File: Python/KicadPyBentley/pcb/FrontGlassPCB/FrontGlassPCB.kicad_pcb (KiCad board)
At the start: 4 copper layers, 177.3 x 82.5 mm, 69 parts

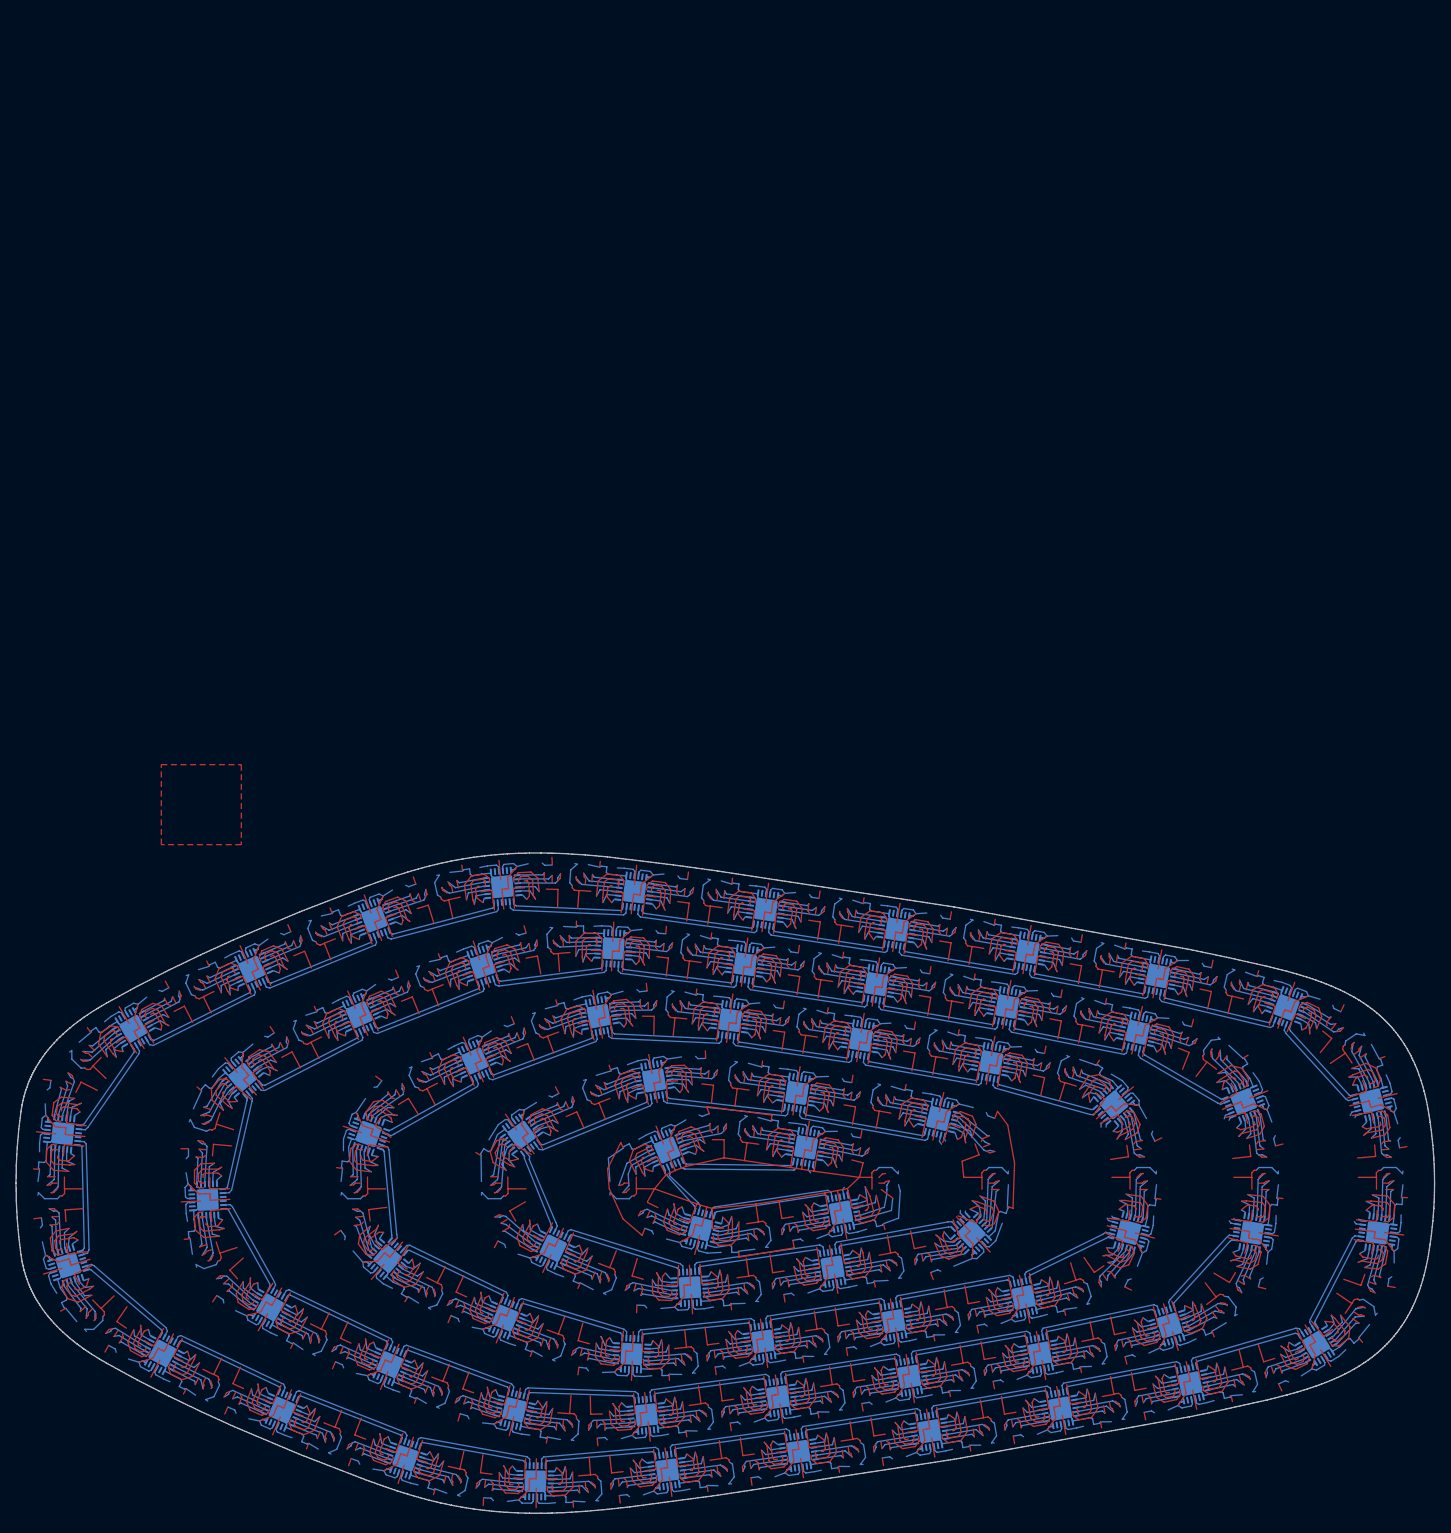
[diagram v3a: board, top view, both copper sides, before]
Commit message: added new footprints
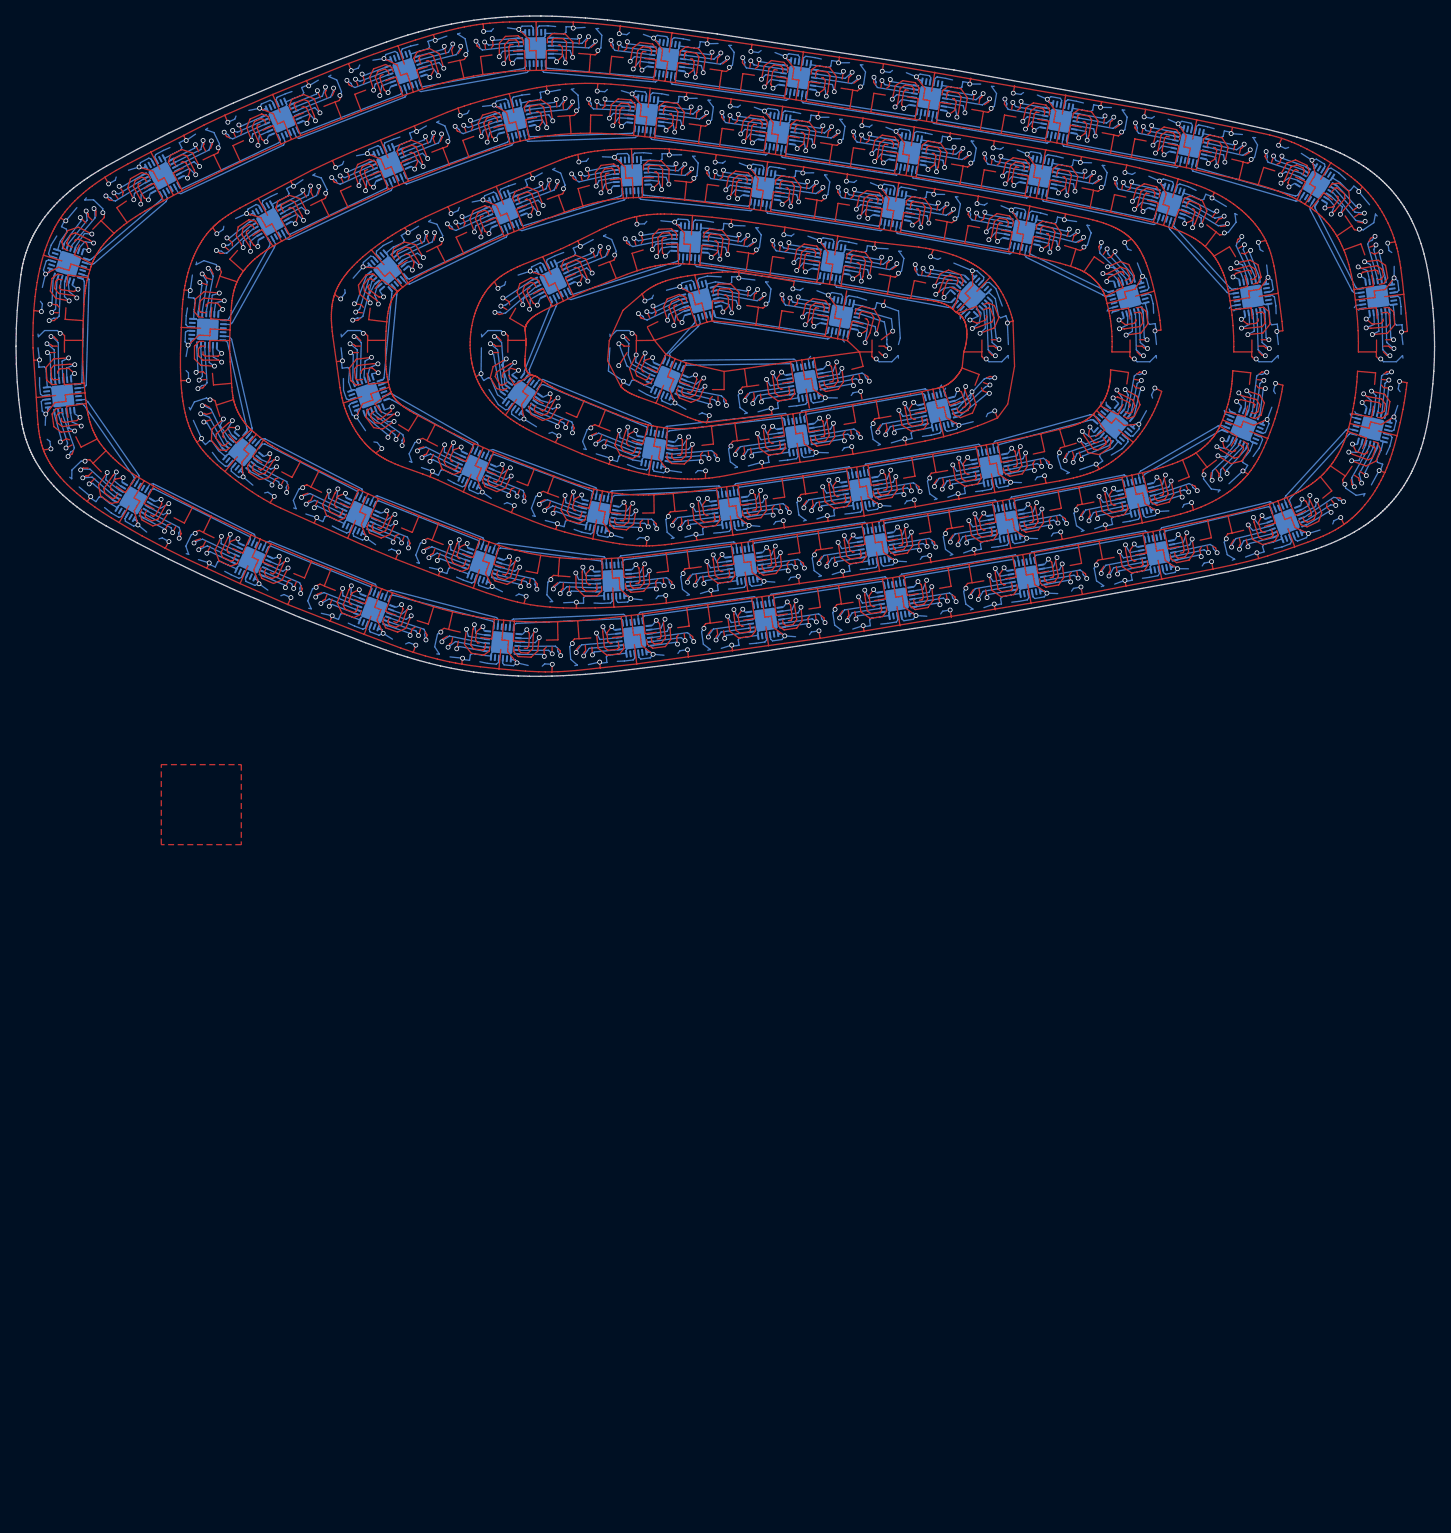
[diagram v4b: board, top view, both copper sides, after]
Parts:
- removed the REF** at (101.3, 58.6)
- removed the REF** at (107.8, 66.6)
- removed the REF** at (91.5, 69.6)
- removed the REF** at (75.2, 72.1)
- removed the REF** at (58.8, 73.7)
- removed the REF** at (43.0, 69.2)
- removed the REF** at (28.3, 61.8)
- removed the REF** at (25.9, 46.2)
- removed the REF** at (39.2, 37.0)
- removed the REF** at (54.7, 31.4)
- removed the REF** at (71.1, 31.9)
- removed the REF** at (83.9, 62.9)
- removed the REF** at (87.5, 34.4)
- removed the REF** at (103.7, 37.2)
- removed the REF** at (119.1, 42.5)
- removed the REF** at (136.3, 58.5)
- removed the REF** at (126.0, 70.1)
- removed the REF** at (109.8, 73.6)
- removed the REF** at (93.5, 76.5)
- removed the REF** at (77.1, 79.1)
- removed the REF** at (60.6, 81.3)
- removed the REF** at (44.1, 80.6)
- removed the REF** at (66.1, 65.4)
- removed the REF** at (28.6, 75.0)
- removed the REF** at (13.6, 67.8)
- removed the REF** at (5.79, 54.4)
- removed the REF** at (10.2, 39.1)
- removed the REF** at (24.8, 31.3)
- removed the REF** at (40.2, 25.1)
- removed the REF** at (56.5, 23.0)
- removed the REF** at (73.0, 25.0)
- removed the REF** at (89.4, 27.4)
- removed the REF** at (105.7, 30.2)
- removed the REF** at (49.0, 60.5)
- removed the REF** at (122.0, 33.5)
- removed the REF** at (135.3, 42.1)
- removed the REF** at (152.0, 58.5)
- removed the REF** at (144.4, 72.5)
- removed the REF** at (128.6, 77.4)
- removed the REF** at (112.3, 80.5)
- removed the REF** at (96.0, 83.3)
- removed the REF** at (79.7, 85.9)
- removed the REF** at (63.3, 88.2)
- removed the REF** at (46.8, 89.6)
- removed the REF** at (45.0, 46.3)
- removed the REF** at (30.5, 86.7)
- removed the REF** at (15.1, 80.7)
- removed the REF** at (0.14, 73.6)
- removed the REF** at (-11.6, 62.6)
- removed the REF** at (-12.3, 46.1)
- removed the REF** at (-3.49, 33.0)
- removed the REF** at (11.3, 25.6)
- removed the REF** at (26.6, 19.3)
- removed the REF** at (42.6, 15.3)
- removed the REF** at (59.2, 15.9)
- removed the REF** at (61.6, 39.5)
- removed the REF** at (75.6, 18.1)
- removed the REF** at (91.9, 20.6)
- removed the REF** at (108.3, 23.4)
- removed the REF** at (124.6, 26.4)
- removed the REF** at (140.6, 30.4)
- removed the REF** at (151.3, 42.0)
- removed the REF** at (85.0, 56.0)
- removed the REF** at (67.4, 58.0)
- removed the REF** at (63.2, 48.2)
- removed the REF** at (80.6, 47.8)
- removed the REF** at (79.5, 41.0)
- removed the REF** at (97.2, 44.2)
- removed the REF** at (120.9, 58.4)
- added REF**: Texas_RGE0024H_EP2.7x2.7mm, Texas_RGE0024H_EP2.7x2.7mm, B.Cu at (101.3, -58.6)
- added REF**: Texas_RGE0024H_EP2.7x2.7mm, Texas_RGE0024H_EP2.7x2.7mm, B.Cu at (107.8, -66.6)
- added REF**: Texas_RGE0024H_EP2.7x2.7mm, Texas_RGE0024H_EP2.7x2.7mm, B.Cu at (91.5, -69.6)
- added REF**: Texas_RGE0024H_EP2.7x2.7mm, Texas_RGE0024H_EP2.7x2.7mm, B.Cu at (75.2, -72.1)
- added REF**: Texas_RGE0024H_EP2.7x2.7mm, Texas_RGE0024H_EP2.7x2.7mm, B.Cu at (58.8, -73.7)
- added REF**: Texas_RGE0024H_EP2.7x2.7mm, Texas_RGE0024H_EP2.7x2.7mm, B.Cu at (43.0, -69.2)
- added REF**: Texas_RGE0024H_EP2.7x2.7mm, Texas_RGE0024H_EP2.7x2.7mm, B.Cu at (28.3, -61.8)
- added REF**: Texas_RGE0024H_EP2.7x2.7mm, Texas_RGE0024H_EP2.7x2.7mm, B.Cu at (25.9, -46.2)
- added REF**: Texas_RGE0024H_EP2.7x2.7mm, Texas_RGE0024H_EP2.7x2.7mm, B.Cu at (39.2, -37.0)
- added REF**: Texas_RGE0024H_EP2.7x2.7mm, Texas_RGE0024H_EP2.7x2.7mm, B.Cu at (54.7, -31.4)
- added REF**: Texas_RGE0024H_EP2.7x2.7mm, Texas_RGE0024H_EP2.7x2.7mm, B.Cu at (71.1, -31.9)
- added REF**: Texas_RGE0024H_EP2.7x2.7mm, Texas_RGE0024H_EP2.7x2.7mm, B.Cu at (83.9, -62.9)
- added REF**: Texas_RGE0024H_EP2.7x2.7mm, Texas_RGE0024H_EP2.7x2.7mm, B.Cu at (87.5, -34.4)
- added REF**: Texas_RGE0024H_EP2.7x2.7mm, Texas_RGE0024H_EP2.7x2.7mm, B.Cu at (103.7, -37.2)
- added REF**: Texas_RGE0024H_EP2.7x2.7mm, Texas_RGE0024H_EP2.7x2.7mm, B.Cu at (119.1, -42.5)
- added REF**: Texas_RGE0024H_EP2.7x2.7mm, Texas_RGE0024H_EP2.7x2.7mm, B.Cu at (136.3, -58.5)
- added REF**: Texas_RGE0024H_EP2.7x2.7mm, Texas_RGE0024H_EP2.7x2.7mm, B.Cu at (126.0, -70.1)
- added REF**: Texas_RGE0024H_EP2.7x2.7mm, Texas_RGE0024H_EP2.7x2.7mm, B.Cu at (109.8, -73.6)
- added REF**: Texas_RGE0024H_EP2.7x2.7mm, Texas_RGE0024H_EP2.7x2.7mm, B.Cu at (93.5, -76.5)
- added REF**: Texas_RGE0024H_EP2.7x2.7mm, Texas_RGE0024H_EP2.7x2.7mm, B.Cu at (77.1, -79.1)
- added REF**: Texas_RGE0024H_EP2.7x2.7mm, Texas_RGE0024H_EP2.7x2.7mm, B.Cu at (60.6, -81.3)
- added REF**: Texas_RGE0024H_EP2.7x2.7mm, Texas_RGE0024H_EP2.7x2.7mm, B.Cu at (44.1, -80.6)
- added REF**: Texas_RGE0024H_EP2.7x2.7mm, Texas_RGE0024H_EP2.7x2.7mm, B.Cu at (66.1, -65.4)
- added REF**: Texas_RGE0024H_EP2.7x2.7mm, Texas_RGE0024H_EP2.7x2.7mm, B.Cu at (28.6, -75.0)
- added REF**: Texas_RGE0024H_EP2.7x2.7mm, Texas_RGE0024H_EP2.7x2.7mm, B.Cu at (13.6, -67.8)
- added REF**: Texas_RGE0024H_EP2.7x2.7mm, Texas_RGE0024H_EP2.7x2.7mm, B.Cu at (5.79, -54.4)
- added REF**: Texas_RGE0024H_EP2.7x2.7mm, Texas_RGE0024H_EP2.7x2.7mm, B.Cu at (10.2, -39.1)
- added REF**: Texas_RGE0024H_EP2.7x2.7mm, Texas_RGE0024H_EP2.7x2.7mm, B.Cu at (24.8, -31.3)
- added REF**: Texas_RGE0024H_EP2.7x2.7mm, Texas_RGE0024H_EP2.7x2.7mm, B.Cu at (40.2, -25.1)
- added REF**: Texas_RGE0024H_EP2.7x2.7mm, Texas_RGE0024H_EP2.7x2.7mm, B.Cu at (56.5, -23.0)
- added REF**: Texas_RGE0024H_EP2.7x2.7mm, Texas_RGE0024H_EP2.7x2.7mm, B.Cu at (73.0, -25.0)
- added REF**: Texas_RGE0024H_EP2.7x2.7mm, Texas_RGE0024H_EP2.7x2.7mm, B.Cu at (89.4, -27.4)
- added REF**: Texas_RGE0024H_EP2.7x2.7mm, Texas_RGE0024H_EP2.7x2.7mm, B.Cu at (105.7, -30.2)
- added REF**: Texas_RGE0024H_EP2.7x2.7mm, Texas_RGE0024H_EP2.7x2.7mm, B.Cu at (49.0, -60.5)
- added REF**: Texas_RGE0024H_EP2.7x2.7mm, Texas_RGE0024H_EP2.7x2.7mm, B.Cu at (122.0, -33.5)
- added REF**: Texas_RGE0024H_EP2.7x2.7mm, Texas_RGE0024H_EP2.7x2.7mm, B.Cu at (135.3, -42.1)
- added REF**: Texas_RGE0024H_EP2.7x2.7mm, Texas_RGE0024H_EP2.7x2.7mm, B.Cu at (152.0, -58.5)
- added REF**: Texas_RGE0024H_EP2.7x2.7mm, Texas_RGE0024H_EP2.7x2.7mm, B.Cu at (144.4, -72.5)
- added REF**: Texas_RGE0024H_EP2.7x2.7mm, Texas_RGE0024H_EP2.7x2.7mm, B.Cu at (128.6, -77.4)
- added REF**: Texas_RGE0024H_EP2.7x2.7mm, Texas_RGE0024H_EP2.7x2.7mm, B.Cu at (112.3, -80.5)
- added REF**: Texas_RGE0024H_EP2.7x2.7mm, Texas_RGE0024H_EP2.7x2.7mm, B.Cu at (96.0, -83.3)
- added REF**: Texas_RGE0024H_EP2.7x2.7mm, Texas_RGE0024H_EP2.7x2.7mm, B.Cu at (79.7, -85.9)
- added REF**: Texas_RGE0024H_EP2.7x2.7mm, Texas_RGE0024H_EP2.7x2.7mm, B.Cu at (63.3, -88.2)
- added REF**: Texas_RGE0024H_EP2.7x2.7mm, Texas_RGE0024H_EP2.7x2.7mm, B.Cu at (46.8, -89.6)
- added REF**: Texas_RGE0024H_EP2.7x2.7mm, Texas_RGE0024H_EP2.7x2.7mm, B.Cu at (45.0, -46.3)
- added REF**: Texas_RGE0024H_EP2.7x2.7mm, Texas_RGE0024H_EP2.7x2.7mm, B.Cu at (30.5, -86.7)
- added REF**: Texas_RGE0024H_EP2.7x2.7mm, Texas_RGE0024H_EP2.7x2.7mm, B.Cu at (15.1, -80.7)
- added REF**: Texas_RGE0024H_EP2.7x2.7mm, Texas_RGE0024H_EP2.7x2.7mm, B.Cu at (0.14, -73.6)
- added REF**: Texas_RGE0024H_EP2.7x2.7mm, Texas_RGE0024H_EP2.7x2.7mm, B.Cu at (-11.6, -62.6)
- added REF**: Texas_RGE0024H_EP2.7x2.7mm, Texas_RGE0024H_EP2.7x2.7mm, B.Cu at (-12.3, -46.1)
- added REF**: Texas_RGE0024H_EP2.7x2.7mm, Texas_RGE0024H_EP2.7x2.7mm, B.Cu at (-3.49, -33.0)
- added REF**: Texas_RGE0024H_EP2.7x2.7mm, Texas_RGE0024H_EP2.7x2.7mm, B.Cu at (11.3, -25.6)
- added REF**: Texas_RGE0024H_EP2.7x2.7mm, Texas_RGE0024H_EP2.7x2.7mm, B.Cu at (26.6, -19.3)
- added REF**: Texas_RGE0024H_EP2.7x2.7mm, Texas_RGE0024H_EP2.7x2.7mm, B.Cu at (42.6, -15.3)
- added REF**: Texas_RGE0024H_EP2.7x2.7mm, Texas_RGE0024H_EP2.7x2.7mm, B.Cu at (59.2, -15.9)
- added REF**: Texas_RGE0024H_EP2.7x2.7mm, Texas_RGE0024H_EP2.7x2.7mm, B.Cu at (61.6, -39.5)
- added REF**: Texas_RGE0024H_EP2.7x2.7mm, Texas_RGE0024H_EP2.7x2.7mm, B.Cu at (75.6, -18.1)
- added REF**: Texas_RGE0024H_EP2.7x2.7mm, Texas_RGE0024H_EP2.7x2.7mm, B.Cu at (91.9, -20.6)
- added REF**: Texas_RGE0024H_EP2.7x2.7mm, Texas_RGE0024H_EP2.7x2.7mm, B.Cu at (108.3, -23.4)
- added REF**: Texas_RGE0024H_EP2.7x2.7mm, Texas_RGE0024H_EP2.7x2.7mm, B.Cu at (124.6, -26.4)
- added REF**: Texas_RGE0024H_EP2.7x2.7mm, Texas_RGE0024H_EP2.7x2.7mm, B.Cu at (140.6, -30.4)
- added REF**: Texas_RGE0024H_EP2.7x2.7mm, Texas_RGE0024H_EP2.7x2.7mm, B.Cu at (151.3, -42.0)
- added REF**: Texas_RGE0024H_EP2.7x2.7mm, Texas_RGE0024H_EP2.7x2.7mm, B.Cu at (85.0, -56.0)
- added REF**: Texas_RGE0024H_EP2.7x2.7mm, Texas_RGE0024H_EP2.7x2.7mm, B.Cu at (67.4, -58.0)
- added REF**: Texas_RGE0024H_EP2.7x2.7mm, Texas_RGE0024H_EP2.7x2.7mm, B.Cu at (63.2, -48.2)
- added REF**: Texas_RGE0024H_EP2.7x2.7mm, Texas_RGE0024H_EP2.7x2.7mm, B.Cu at (80.6, -47.8)
- added REF**: Texas_RGE0024H_EP2.7x2.7mm, Texas_RGE0024H_EP2.7x2.7mm, B.Cu at (79.5, -41.0)
- added REF**: Texas_RGE0024H_EP2.7x2.7mm, Texas_RGE0024H_EP2.7x2.7mm, B.Cu at (97.2, -44.2)
- added REF**: Texas_RGE0024H_EP2.7x2.7mm, Texas_RGE0024H_EP2.7x2.7mm, B.Cu at (120.9, -58.4)
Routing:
- net (no net): track 10402.9 -> 12582.7 mm, vias 0 -> 1104
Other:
- outline, holes or cut-outs redrawn

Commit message: made libraries locally available
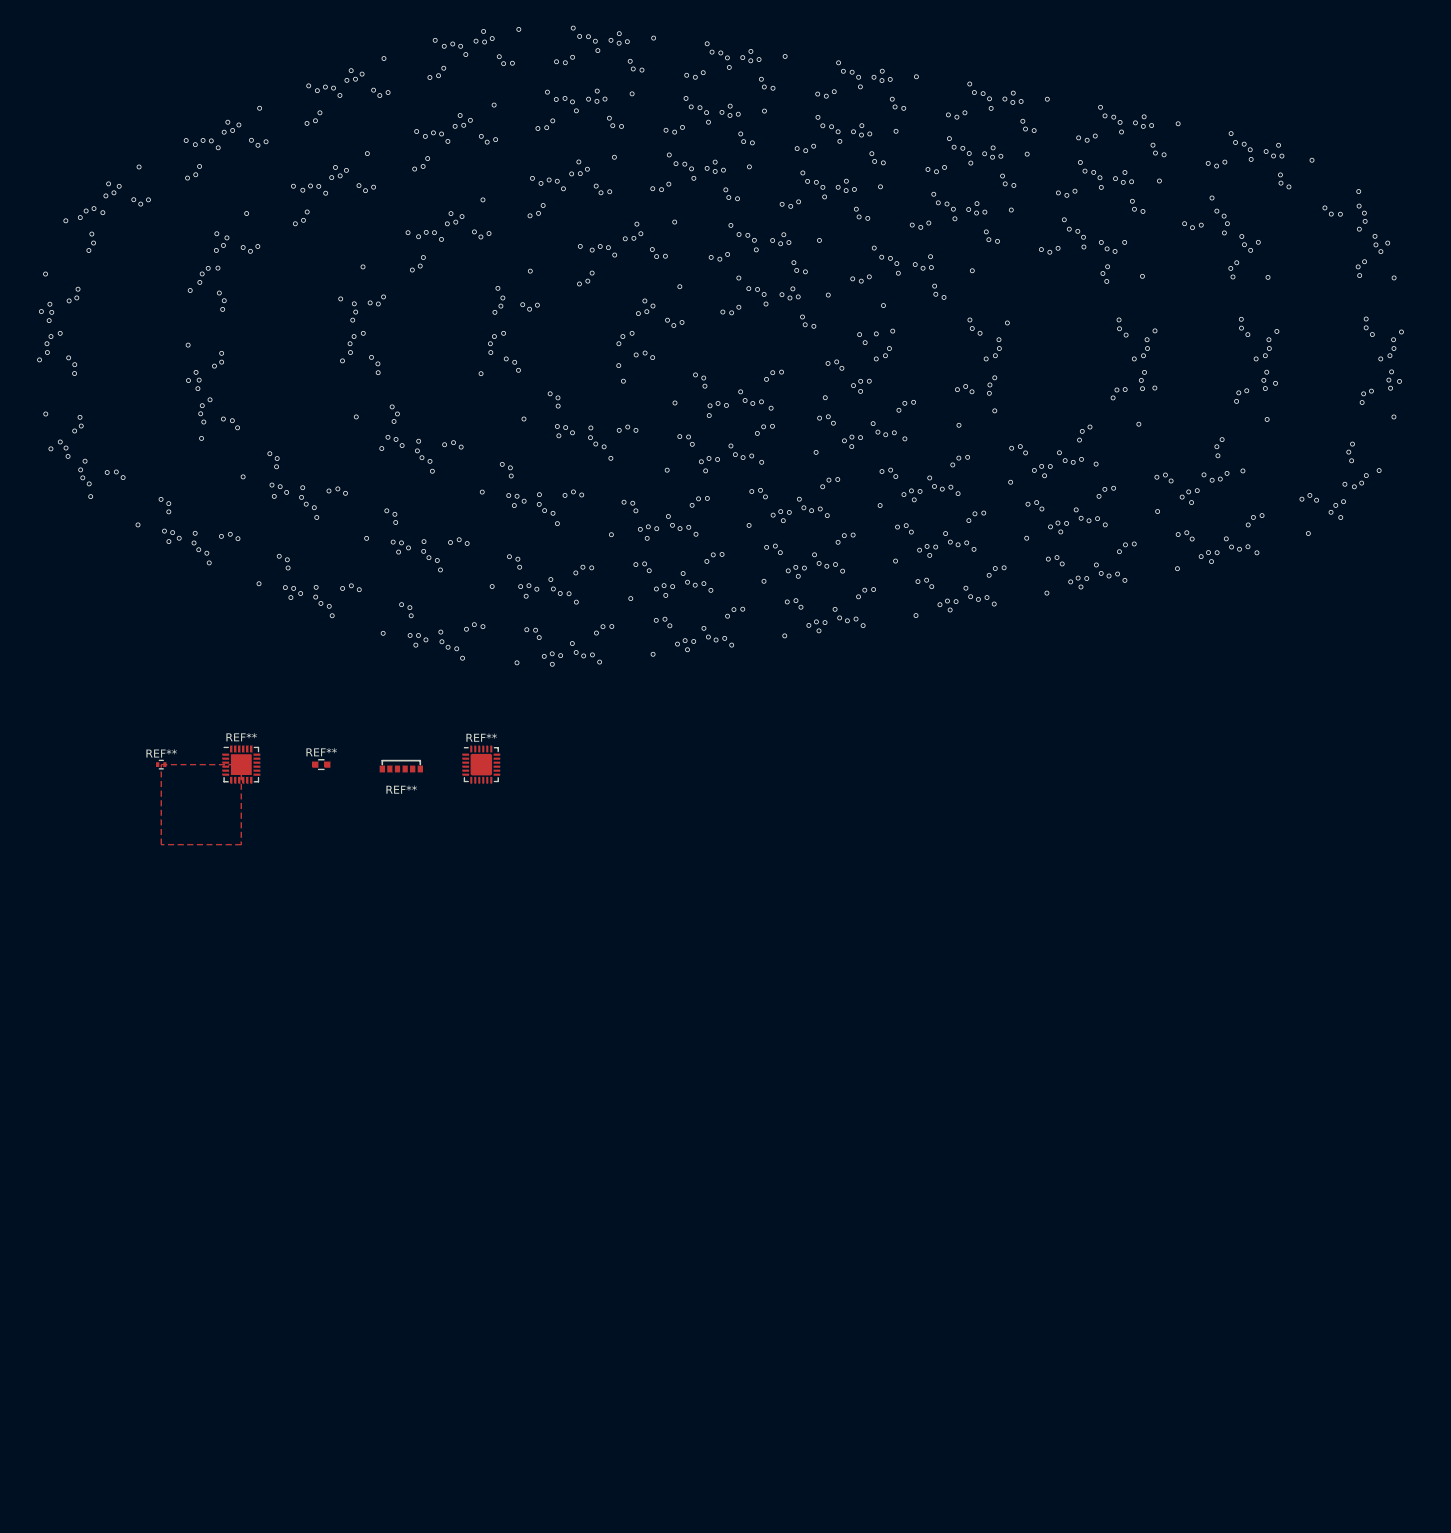
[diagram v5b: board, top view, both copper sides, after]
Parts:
- removed the REF** at (101.3, -58.6)
- removed the REF** at (107.8, -66.6)
- removed the REF** at (91.5, -69.6)
- removed the REF** at (75.2, -72.1)
- removed the REF** at (58.8, -73.7)
- removed the REF** at (43.0, -69.2)
- removed the REF** at (28.3, -61.8)
- removed the REF** at (25.9, -46.2)
- removed the REF** at (39.2, -37.0)
- removed the REF** at (54.7, -31.4)
- removed the REF** at (71.1, -31.9)
- removed the REF** at (83.9, -62.9)
- removed the REF** at (87.5, -34.4)
- removed the REF** at (103.7, -37.2)
- removed the REF** at (119.1, -42.5)
- removed the REF** at (136.3, -58.5)
- removed the REF** at (126.0, -70.1)
- removed the REF** at (109.8, -73.6)
- removed the REF** at (93.5, -76.5)
- removed the REF** at (77.1, -79.1)
- removed the REF** at (60.6, -81.3)
- removed the REF** at (44.1, -80.6)
- removed the REF** at (66.1, -65.4)
- removed the REF** at (28.6, -75.0)
- removed the REF** at (13.6, -67.8)
- removed the REF** at (5.79, -54.4)
- removed the REF** at (10.2, -39.1)
- removed the REF** at (24.8, -31.3)
- removed the REF** at (40.2, -25.1)
- removed the REF** at (56.5, -23.0)
- removed the REF** at (73.0, -25.0)
- removed the REF** at (89.4, -27.4)
- removed the REF** at (105.7, -30.2)
- removed the REF** at (49.0, -60.5)
- removed the REF** at (122.0, -33.5)
- removed the REF** at (135.3, -42.1)
- removed the REF** at (152.0, -58.5)
- removed the REF** at (144.4, -72.5)
- removed the REF** at (128.6, -77.4)
- removed the REF** at (112.3, -80.5)
- removed the REF** at (96.0, -83.3)
- removed the REF** at (79.7, -85.9)
- removed the REF** at (63.3, -88.2)
- removed the REF** at (46.8, -89.6)
- removed the REF** at (45.0, -46.3)
- removed the REF** at (30.5, -86.7)
- removed the REF** at (15.1, -80.7)
- removed the REF** at (0.14, -73.6)
- removed the REF** at (-11.6, -62.6)
- removed the REF** at (-12.3, -46.1)
- removed the REF** at (-3.49, -33.0)
- removed the REF** at (11.3, -25.6)
- removed the REF** at (26.6, -19.3)
- removed the REF** at (42.6, -15.3)
- removed the REF** at (59.2, -15.9)
- removed the REF** at (61.6, -39.5)
- removed the REF** at (75.6, -18.1)
- removed the REF** at (91.9, -20.6)
- removed the REF** at (108.3, -23.4)
- removed the REF** at (124.6, -26.4)
- removed the REF** at (140.6, -30.4)
- removed the REF** at (151.3, -42.0)
- removed the REF** at (85.0, -56.0)
- removed the REF** at (67.4, -58.0)
- removed the REF** at (63.2, -48.2)
- removed the REF** at (80.6, -47.8)
- removed the REF** at (79.5, -41.0)
- removed the REF** at (97.2, -44.2)
- removed the REF** at (120.9, -58.4)
- added REF**: R_0402, R_0402, B.Cu at (0.00, 0.00)
- added REF**: QFN-24-1EP_4x4mm_Pitch0.5mm, QFN-24-1EP_4x4mm_Pitch0.5mm, B.Cu at (10.0, 0.00)
- added REF**: C_0603, C_0603, B.Cu at (20.0, 0.00)
- added REF**: CL-Z891, CL-Z891, B.Cu at (30.0, 0.00)
- added REF**: Texas_RGE0024H_EP2.7x2.7mm, Texas_RGE0024H_EP2.7x2.7mm, B.Cu at (40.0, 0.00)
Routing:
- net (no net): track 12582.7 -> 0.00 mm
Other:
- board outline removed
